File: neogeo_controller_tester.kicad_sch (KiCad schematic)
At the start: 31 parts, among them J1 DA15_Plug, J2 USB_B, J3 UJ20-C-H-C-4-SMT-TR

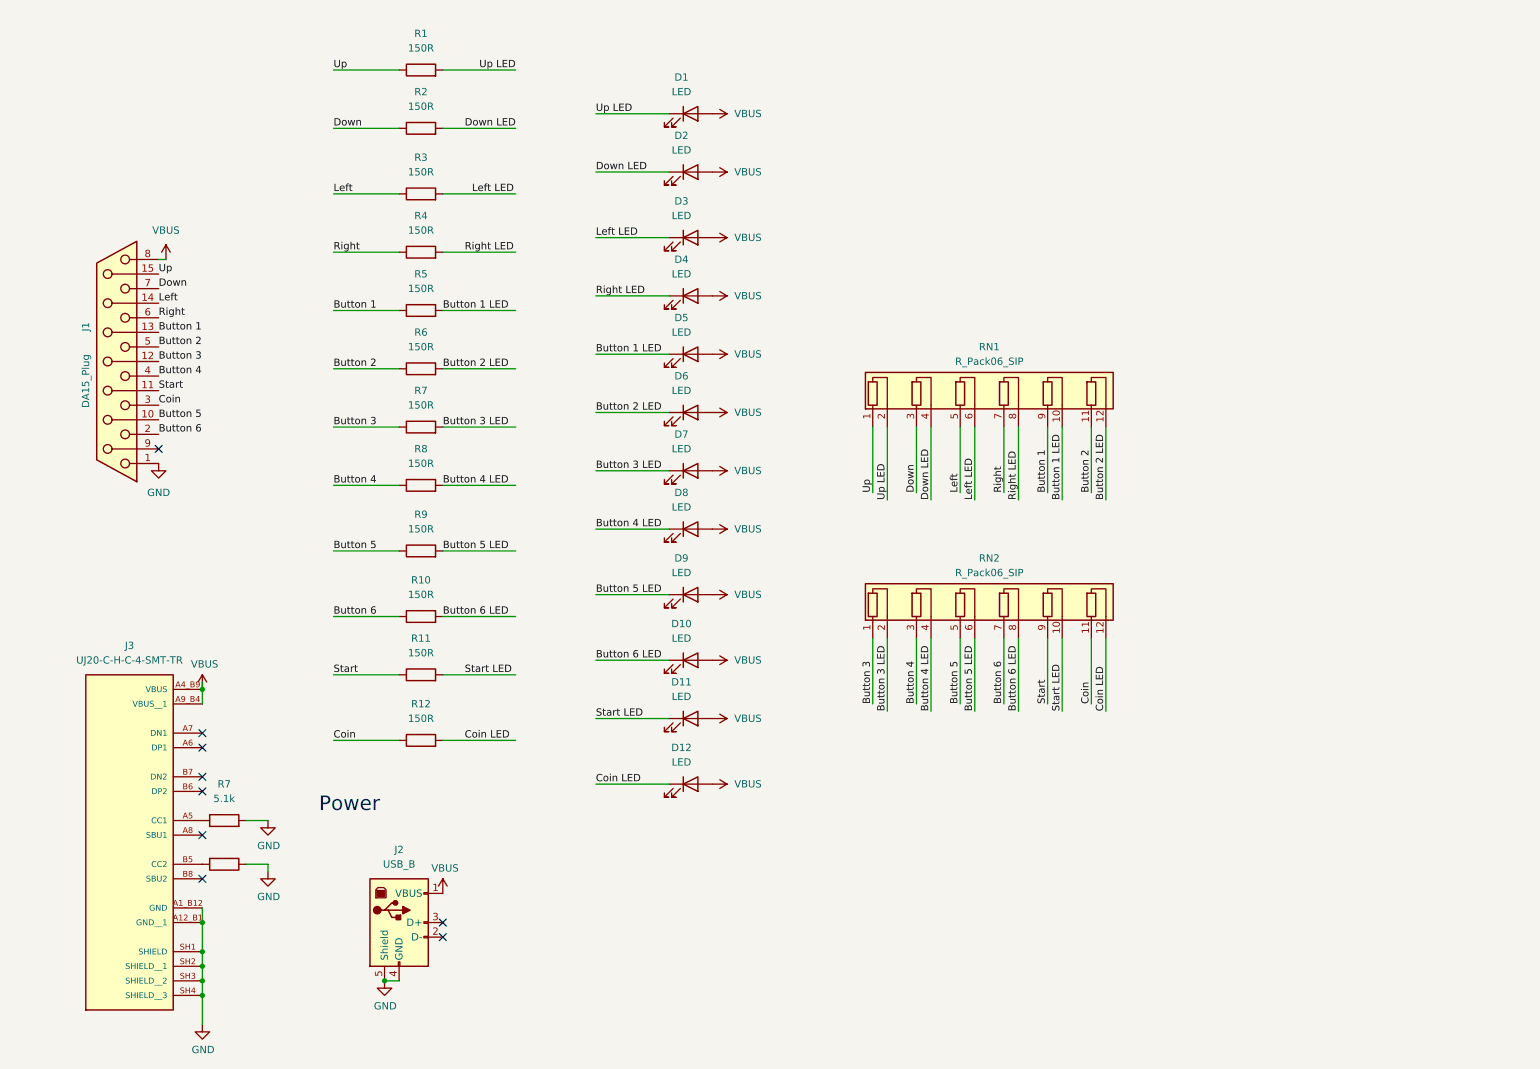
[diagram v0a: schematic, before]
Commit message: Tidy up schematic
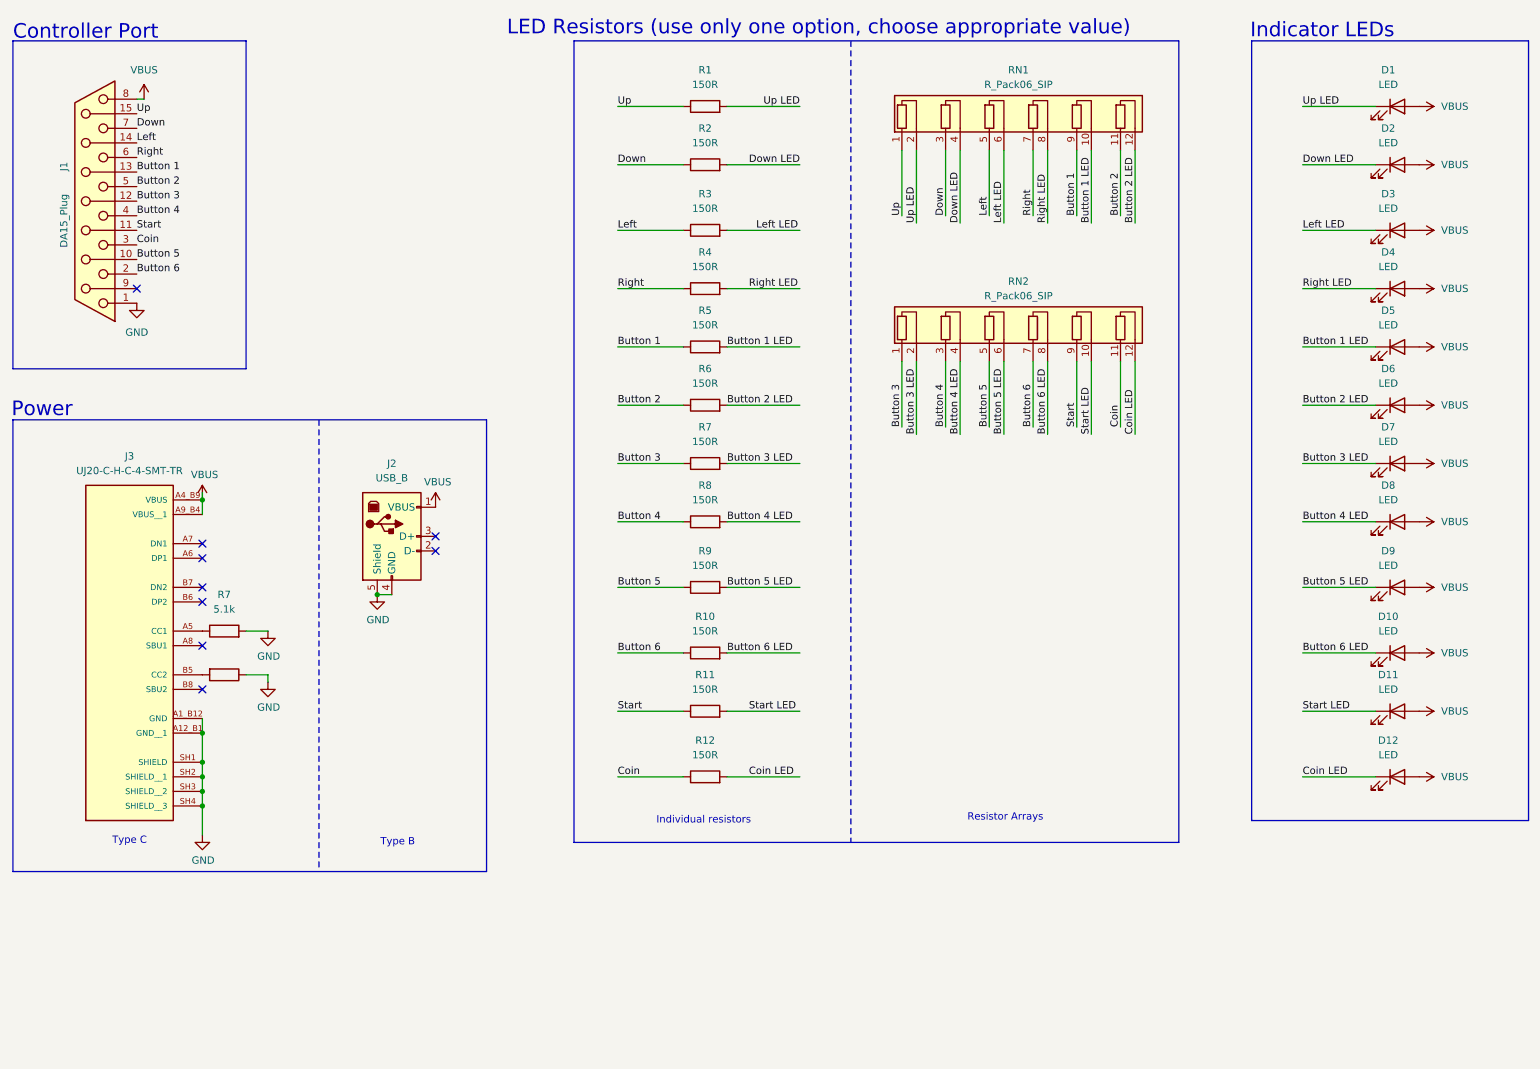
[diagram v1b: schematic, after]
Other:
- note added: "Controller Port"
- note added: "Indicator LEDs"
- note added: "Individual resistors"
- note added: "LED Resistors (use only one option, choose appropriate value)"
- note added: "Resistor Arrays"
- note added: "Type B"
- note added: "Type C"
- title: (none) -> NeoGeo Controller Tester
- moved on the sheet: D1, D10, D11, D12, D2, D3, D4, D5, D6, D7, D8, D9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
